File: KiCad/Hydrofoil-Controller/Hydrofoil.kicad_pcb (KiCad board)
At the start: 2 copper layers, 219.6 x 35 mm, 64 parts, among them J1 Conn_01x03_Pin, J2 Conn_01x03_Pin, Q1 BSS138, Q2 BSS138, Q3 BSS138, Q4 BSS138, Q5 BSS138, U1 ESP32-C3-MINI-1-N4, U2 LD1117S33CTR, U3 TPS22917DBV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

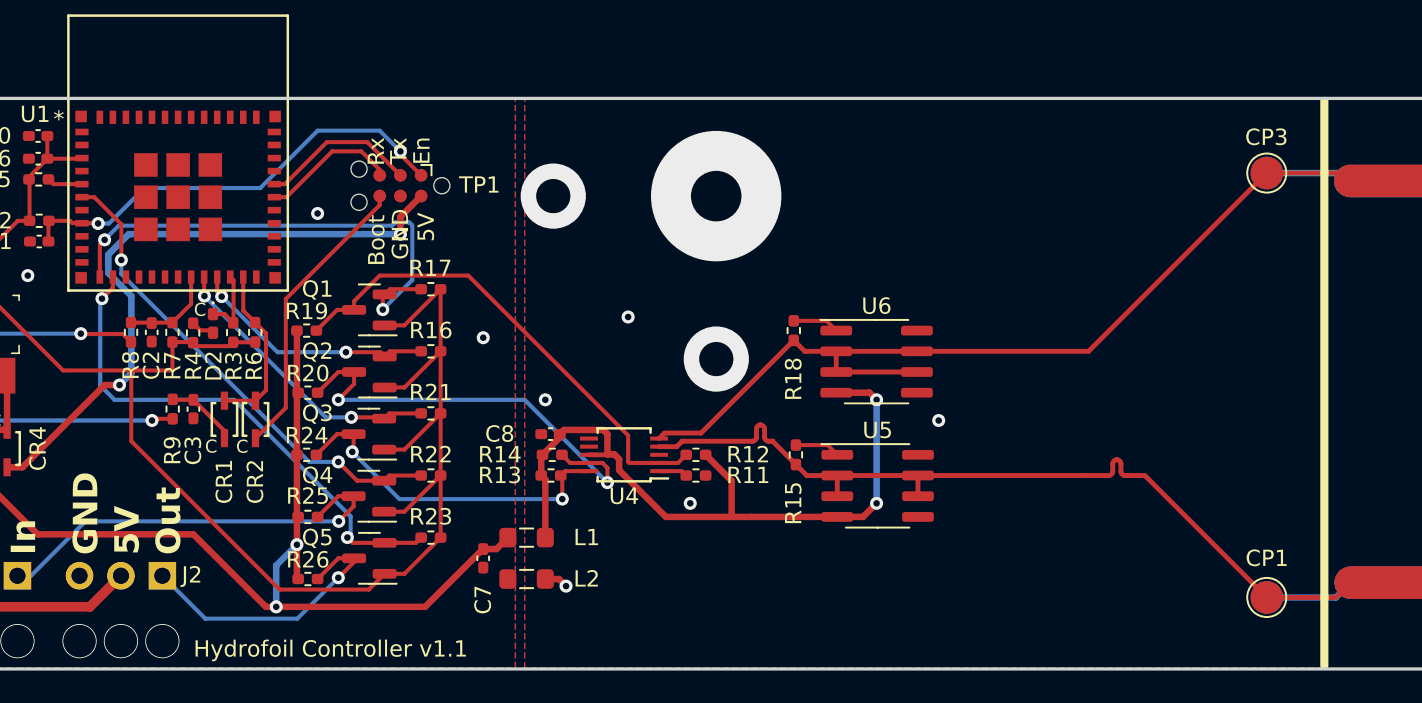
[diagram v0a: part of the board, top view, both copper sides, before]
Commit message: Remove ADC from PCB
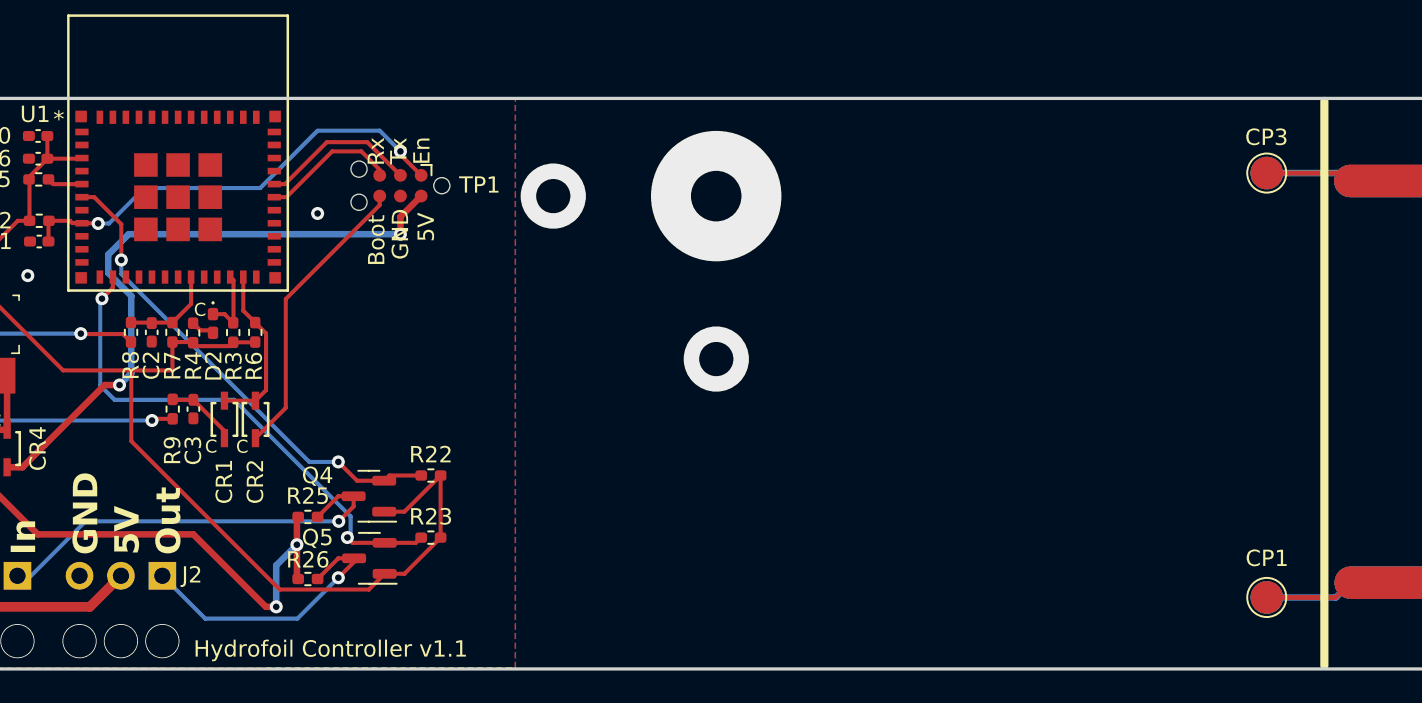
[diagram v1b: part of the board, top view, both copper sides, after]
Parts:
- removed C7, C8: 1u, Capacitor_SMD:C_0402_1005Metric_Pad0.74x0.62mm_HandSolder
- removed L1, L2: MMZ2012Y102B, Inductor_SMD:L_0805_2012Metric_Pad1.05x1.20mm_HandSolder
- removed Q1, Q2, Q3: BSS138, Package_TO_SOT_SMD:SOT-23
- removed R11, R12, R13, R14, R16, R17, R19, R20, R21, R24: 10k, Resistor_SMD:R_0402_1005Metric_Pad0.72x0.64mm_HandSolder
- removed R15, R18: 150R, Resistor_SMD:R_0402_1005Metric_Pad0.72x0.64mm_HandSolder
- removed U4: ADS1115IDGS, Package_SO:TSSOP-10_3x3mm_P0.5mm
- removed U5, U6: LM334M, Package_SO:SOIC-8_3.9x4.9mm_P1.27mm
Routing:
- net AIN1: track 143.1 -> 92.3 mm
- net AIN0: track 164.5 -> 117.5 mm
- net +5VA: track 44.8 -> 0.00 mm, vias 2 -> 0
- net Ready-LV: track 31.1 -> 0.00 mm, vias 2 -> 0
- net Ready-HV: track 30.3 -> 0.00 mm
- net SDA-HV: track 27.5 -> 0.00 mm, vias 2 -> 0
- net +5V: track 67.9 -> 40.6 mm
- net +3.3V: track 105.6 -> 81.1 mm
- net SCL-HV: track 21.3 -> 0.00 mm, vias 2 -> 0
- net SCL-LV: track 17.7 -> 0.00 mm, vias 2 -> 0
- net SDA-LV: track 15.2 -> 0.00 mm, vias 2 -> 0
- net /ADS1115-ADC/Set-Curr-2: track 2.85 -> 0.00 mm
- net /ADS1115-ADC/Set-Curr-1: track 2.79 -> 0.00 mm
- net Net-(U4-ADDR): track 1.77 -> 0.00 mm
- net GNDA: track 211.3 -> 209.8 mm, vias 5 -> 0
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- removed copper zone on B.Cu, net GNDA
- removed copper zone on F.Cu, net GNDA

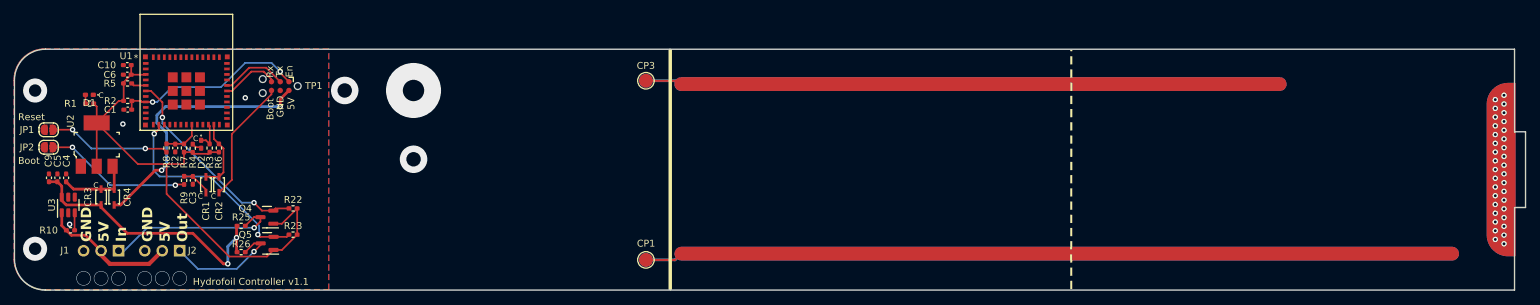
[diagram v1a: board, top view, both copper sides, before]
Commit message: Add capacitance measurement to the PCB
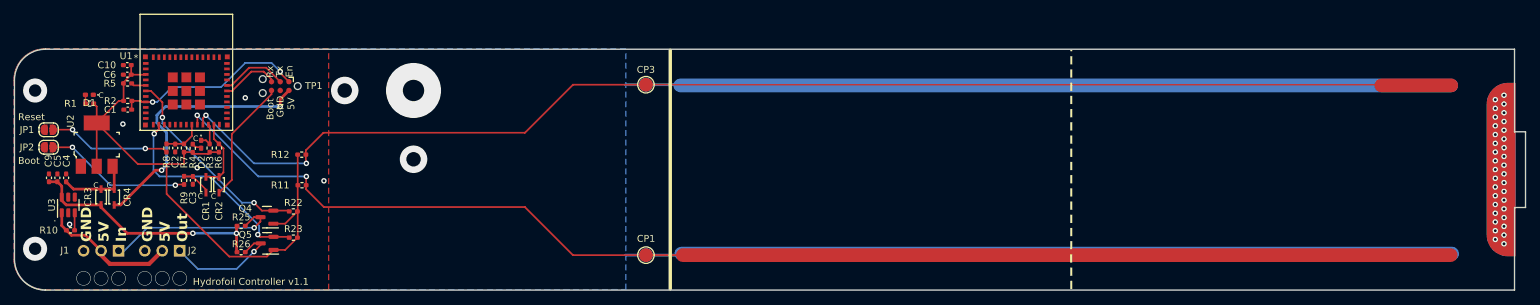
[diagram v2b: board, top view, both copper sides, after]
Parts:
- added R11: 1.4M, Resistor_SMD:R_0402_1005Metric_Pad0.72x0.64mm_HandSolder, F.Cu at (80.6, 91.4)
- added R12: 1.4M, Resistor_SMD:R_0402_1005Metric_Pad0.72x0.64mm_HandSolder, F.Cu at (80.6, 87.0)
- moved CP1 0.70 mm to (130.6, 101.6)
- moved CP2 0.70 mm to (130.6, 101.6)
- moved CP3 0.57 mm to (130.6, 76.8)
- moved CP4 0.57 mm to (130.6, 76.8)
- moved R22 0.44 mm to (79.4, 95.2)
- moved R23 0.44 mm to (79.4, 99.1)
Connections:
- CP1 pad 1: AIN0 -> Cap-Long
- CP2 pad 1: GNDA -> GND
- CP3 pad 1: AIN1 -> Cap-Ref
- CP4 pad 1: GNDA -> GND
- U1 pad 12: Ready-LV -> unconnected-(U1-IO0-Pad12)
- U1 pad 20: SCL-LV -> Cap-Long
- U1 pad 21: SDA-LV -> Cap-Ref
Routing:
- net GND: track 0.00 -> 239.3 mm, vias 3 -> 5
- net GNDA: track 209.8 -> 0.00 mm
- net Cap-Ref: track 0.00 -> 196.5 mm, vias 0 -> 2
- net Cap-Long: track 0.00 -> 192.3 mm, vias 0 -> 2
- net AIN0: track 117.5 -> 0.00 mm
- net AIN1: track 92.3 -> 0.00 mm
- net +3.3V: track 81.1 -> 89.1 mm
- net +5V: track 40.6 -> 35.6 mm
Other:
- board text added: "."
